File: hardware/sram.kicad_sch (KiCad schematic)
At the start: 5 parts, among them U22 IS61C5128AS-25TLI, U25 IS61C5128AS-25TLI

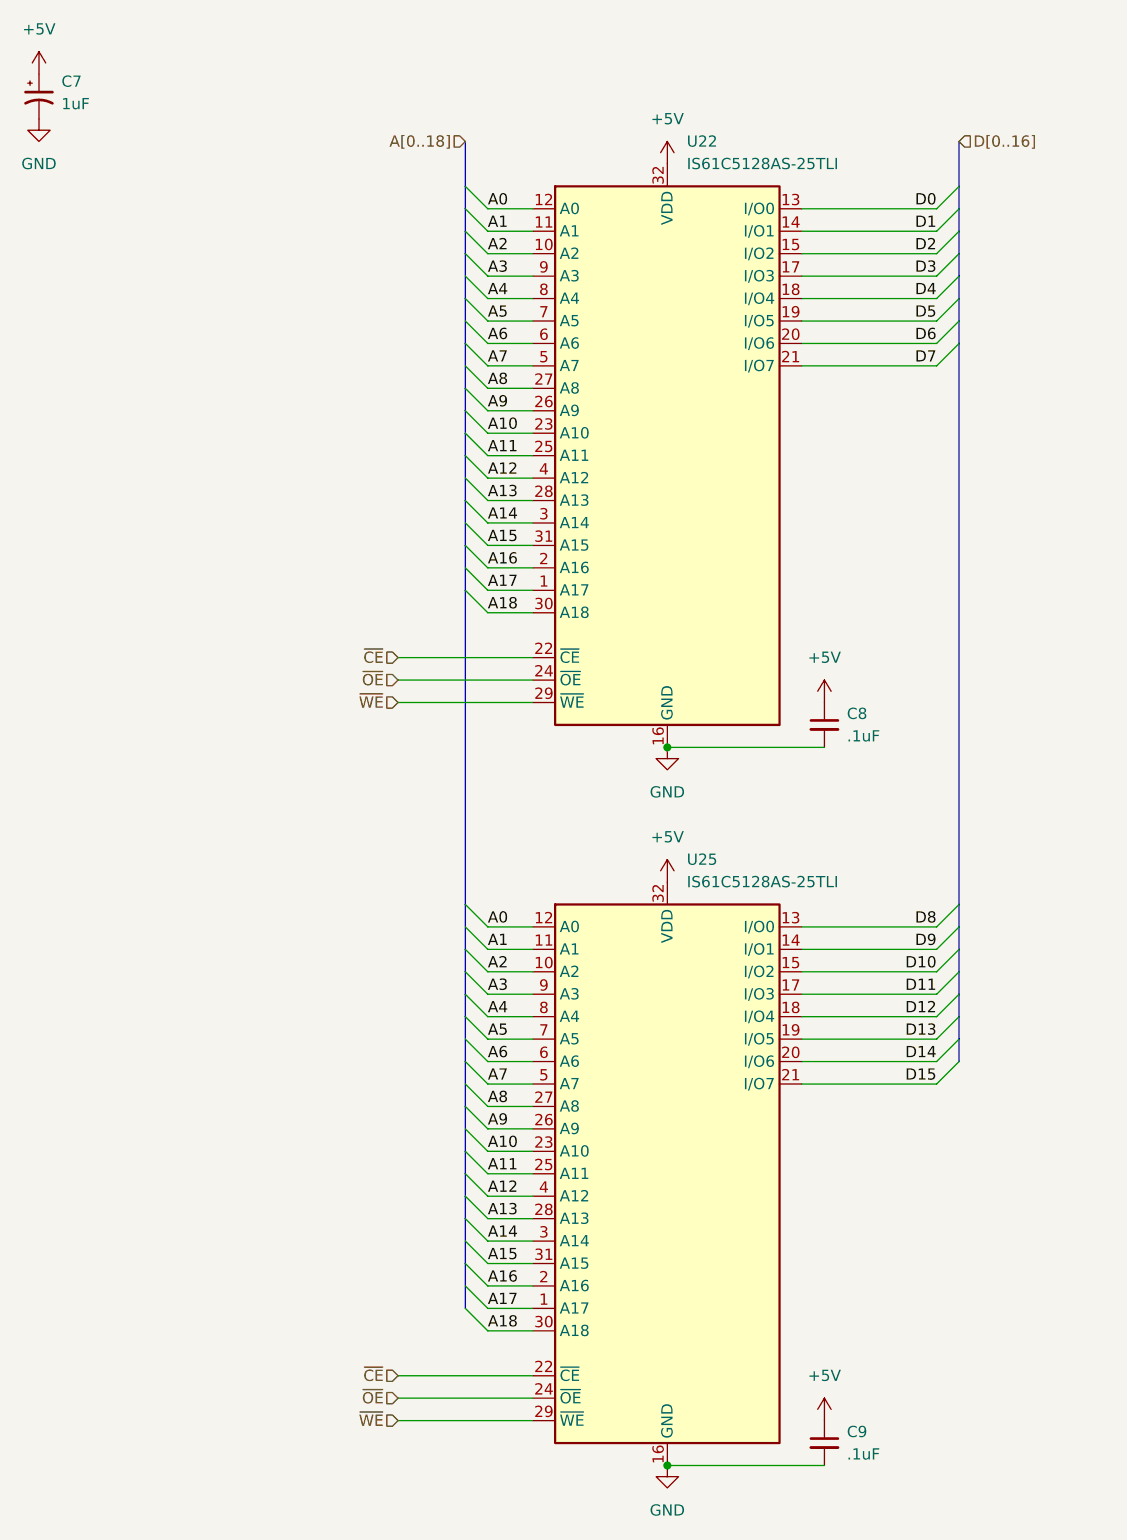
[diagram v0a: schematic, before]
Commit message: add interrupt logic, clean up modules
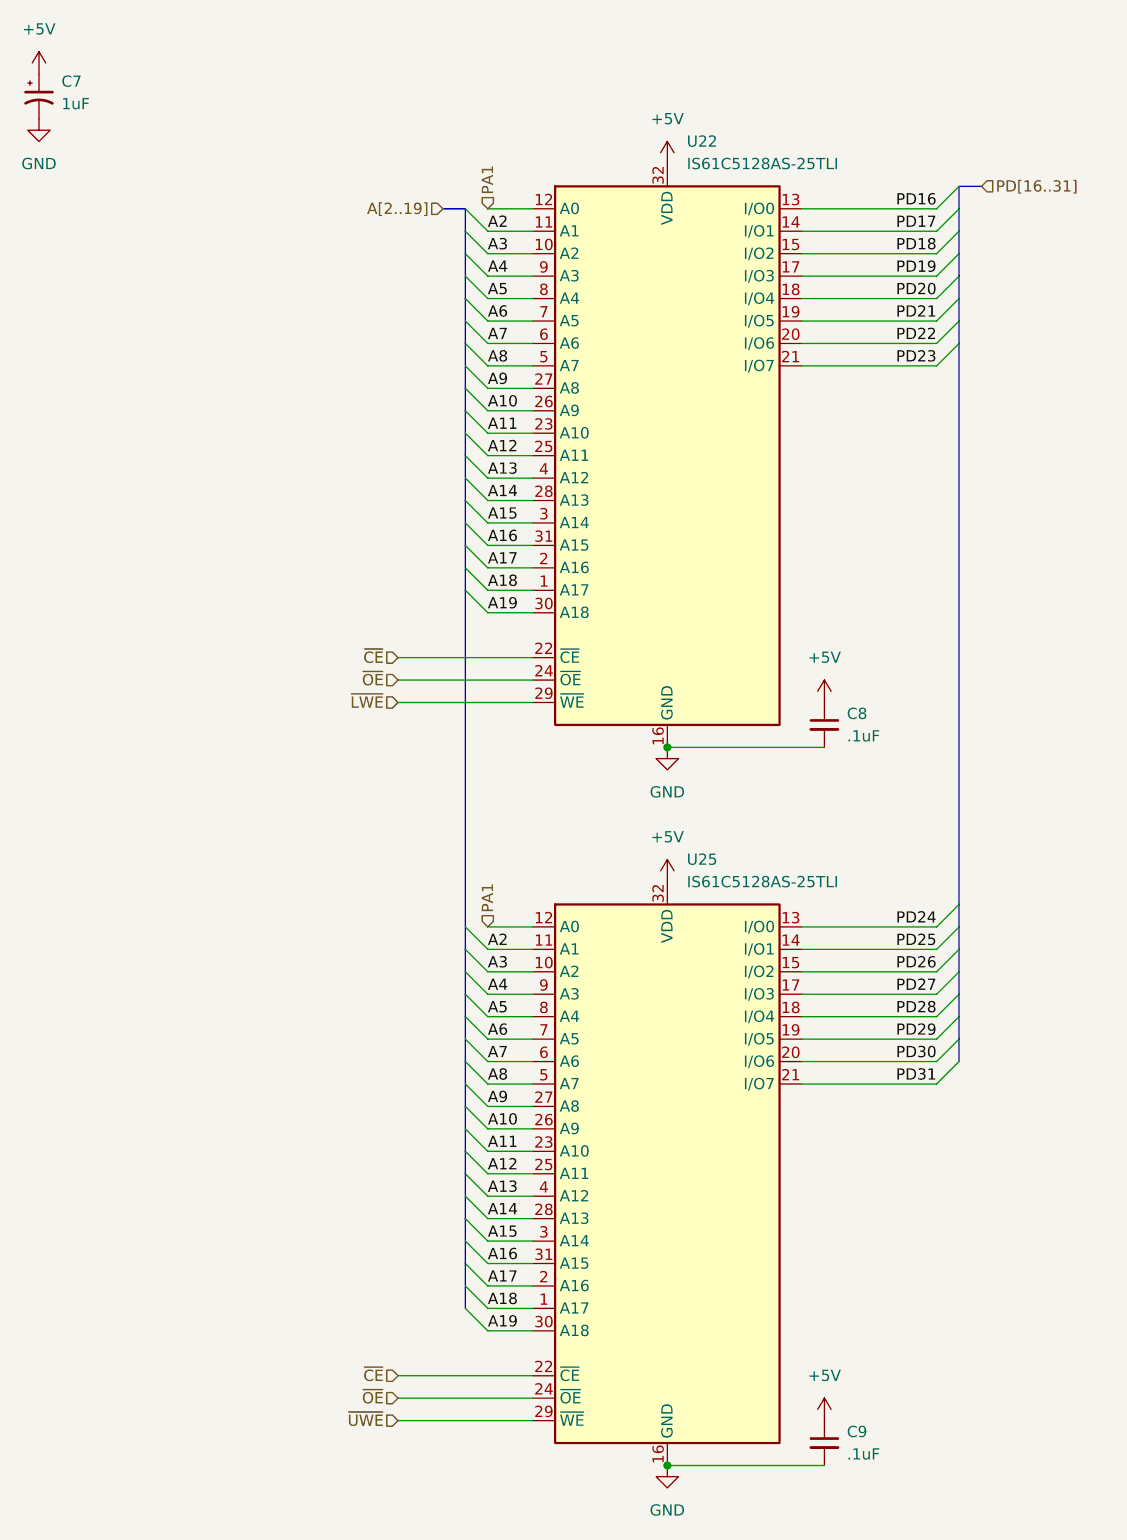
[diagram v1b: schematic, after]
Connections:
- net A1 is gone; now on net A2: U22.11 (A1), U25.11 (A1)
- net A10: now also U22.26 (A9), U25.26 (A9); no longer U22.23 (A10), U25.23 (A10)
- net A11: now also U22.23 (A10), U25.23 (A10); no longer U22.25 (A11), U25.25 (A11)
- net A12: now also U22.25 (A11), U25.25 (A11); no longer U22.4 (A12), U25.4 (A12)
- net A13: now also U22.4 (A12), U25.4 (A12); no longer U22.28 (A13), U25.28 (A13)
- net A14: now also U22.28 (A13), U25.28 (A13); no longer U22.3 (A14), U25.3 (A14)
- net A15: now also U22.3 (A14), U25.3 (A14); no longer U22.31 (A15), U25.31 (A15)
- net A16: now also U22.31 (A15), U25.31 (A15); no longer U22.2 (A16), U25.2 (A16)
- net A17: now also U22.2 (A16), U25.2 (A16); no longer U22.1 (A17), U25.1 (A17)
- net A18: now also U22.1 (A17), U25.1 (A17); no longer U22.30 (A18), U25.30 (A18)
- net A2: no longer U22.10 (A2), U25.10 (A2)
- net A3: now also U22.10 (A2), U25.10 (A2); no longer U22.9 (A3), U25.9 (A3)
- net A4: now also U22.9 (A3), U25.9 (A3); no longer U22.8 (A4), U25.8 (A4)
- net A5: now also U22.8 (A4), U25.8 (A4); no longer U22.7 (A5), U25.7 (A5)
- net A6: now also U22.7 (A5), U25.7 (A5); no longer U22.6 (A6), U25.6 (A6)
- net A7: now also U22.6 (A6), U25.6 (A6); no longer U22.5 (A7), U25.5 (A7)
- net A8: now also U22.5 (A7), U25.5 (A7); no longer U22.27 (A8), U25.27 (A8)
- net A9: now also U22.27 (A8), U25.27 (A8); no longer U22.26 (A9), U25.26 (A9)
- net A0 renamed PA1
- net D0 renamed PD16
- net D1 renamed PD17
- net D10 renamed PD26
- net D11 renamed PD27
- net D12 renamed PD28
- net D13 renamed PD29
- net D14 renamed PD30
- net D15 renamed PD31
- net D2 renamed PD18
- net D3 renamed PD19
- net D4 renamed PD20
- net D5 renamed PD21
- net D6 renamed PD22
- net D7 renamed PD23
- net D8 renamed PD24
- net D9 renamed PD25
- net ~{WE} renamed ~{LWE}
- net ~{LWE}: no longer U25.29 (~{WE})
- new net A19: U22.30 (A18), U25.30 (A18)
- new net ~{UWE}: U25.29 (~{WE})
